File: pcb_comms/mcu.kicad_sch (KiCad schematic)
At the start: 28 parts, among them U2 STM32WLE5CCU6, Y3 32MHz

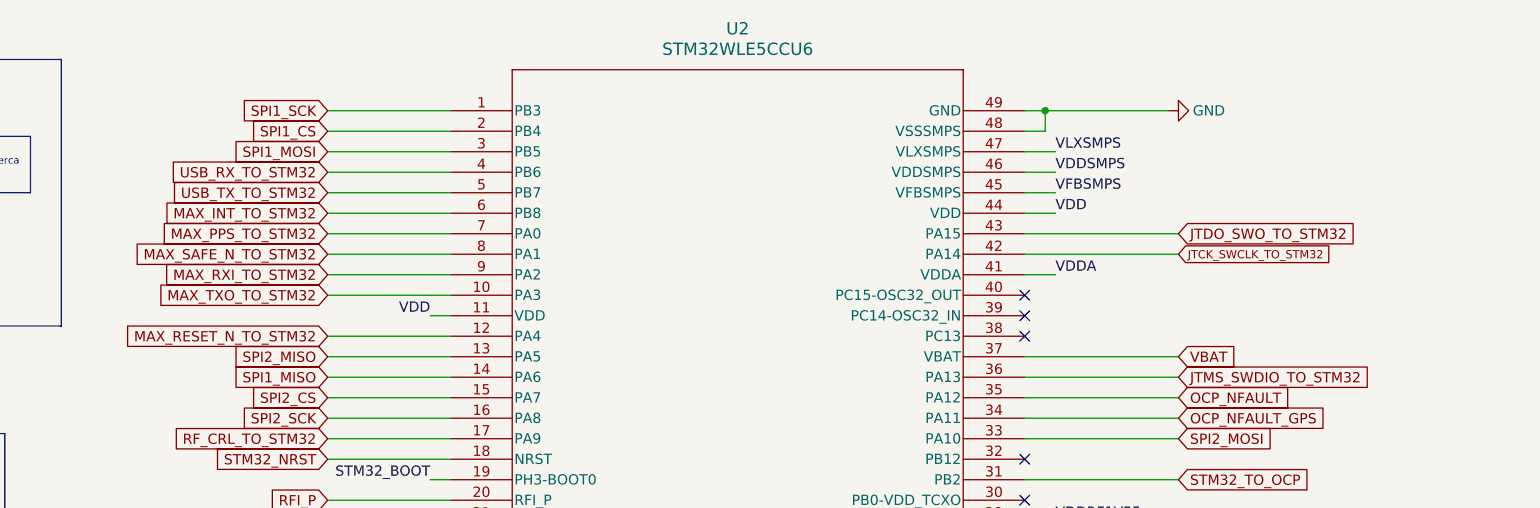
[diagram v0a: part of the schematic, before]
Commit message: Add DRA818
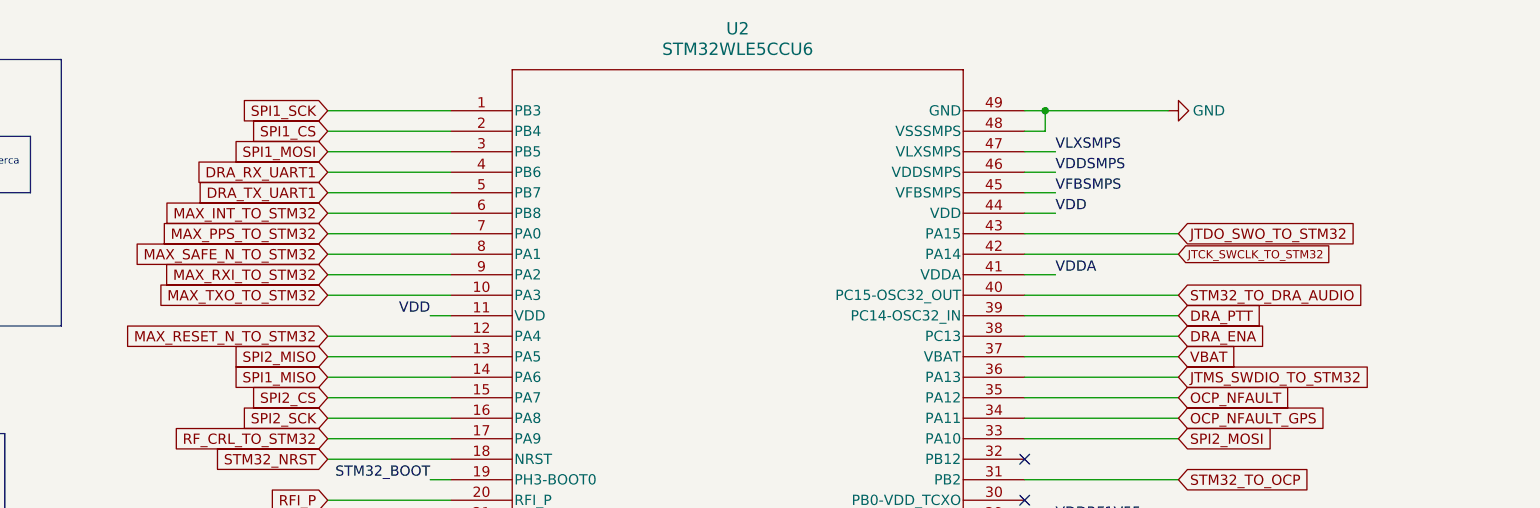
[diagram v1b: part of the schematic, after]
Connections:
- net DRA_ENA: now reaches U2.38 (PC13)
- net DRA_PTT: now reaches U2.39 (PC14-OSC32_IN)
- net STM32_TO_DRA_AUDIO: now reaches U2.40 (PC15-OSC32_OUT)
- net USB_RX_TO_STM32 renamed DRA_RX_UART1
- net USB_TX_TO_STM32 renamed DRA_TX_UART1
- no-connect marks 6 -> 3

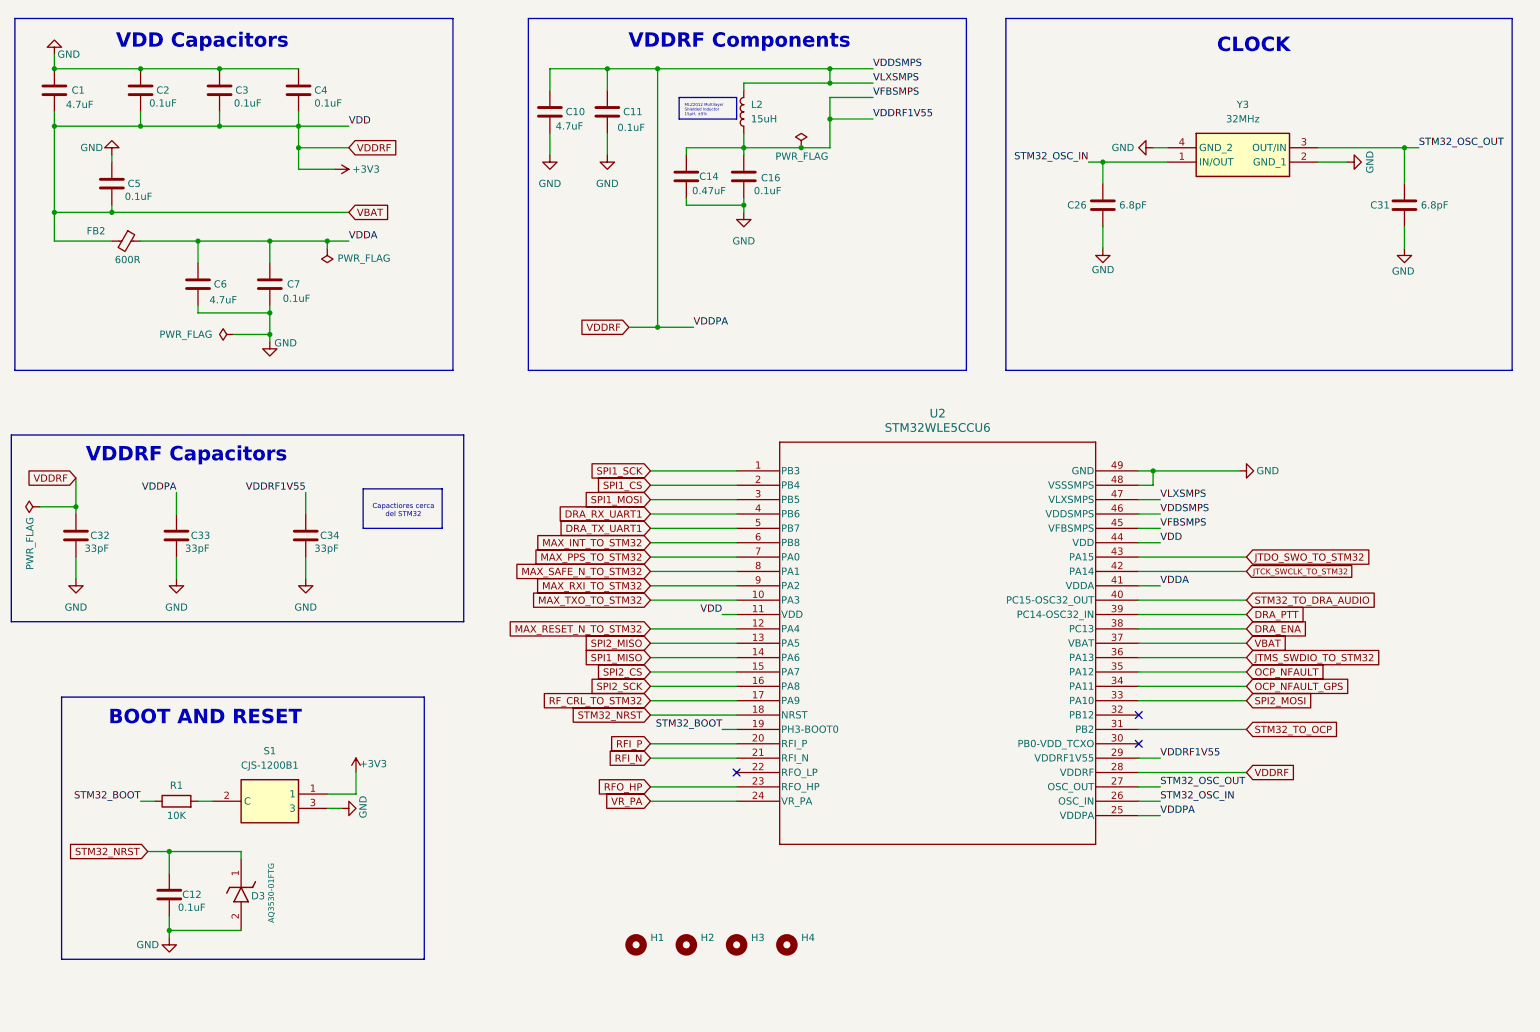
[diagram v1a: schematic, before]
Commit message: remove gps
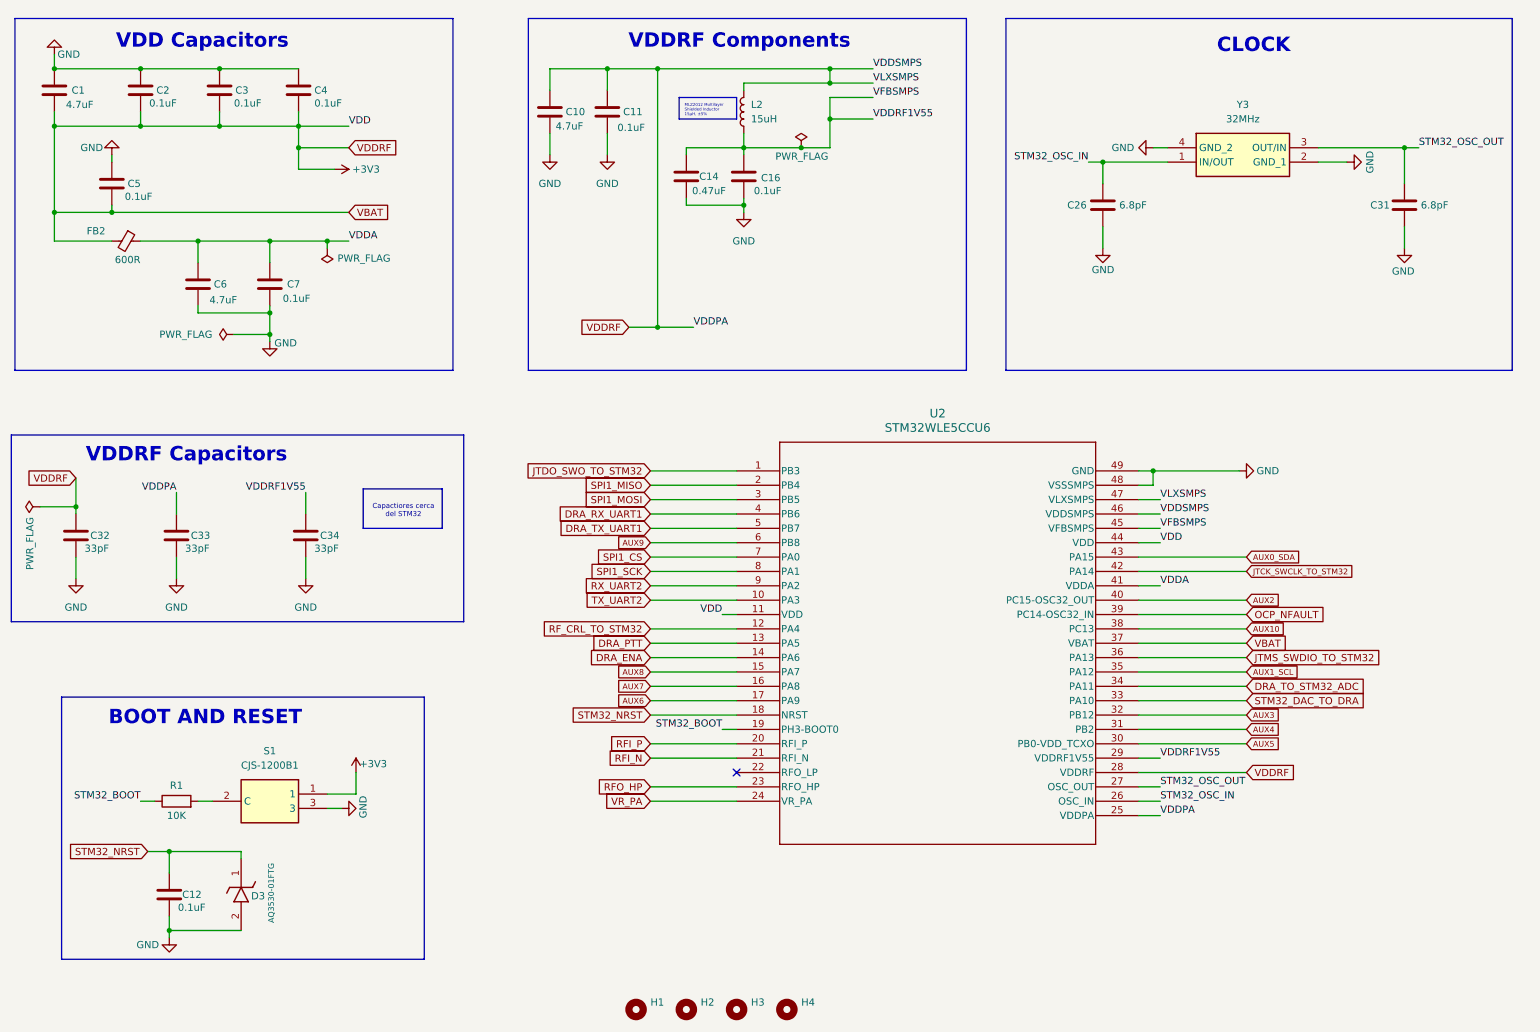
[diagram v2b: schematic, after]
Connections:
- net MAX_PPS_TO_STM32 is gone; now on net SPI1_CS: U2.7 (PA0)
- net MAX_RESET_N_TO_STM32 is gone; now on net RF_CRL_TO_STM32: U2.12 (PA4)
- net MAX_SAFE_N_TO_STM32 is gone; now on net SPI1_SCK: U2.8 (PA1)
- net SPI2_MISO is gone; now on net DRA_PTT: U2.13 (PA5)
- net DRA_ENA: now also U2.14 (PA6); no longer U2.38 (PC13)
- net DRA_PTT: no longer U2.39 (PC14-OSC32_IN)
- net JTDO_SWO_TO_STM32: now also U2.1 (PB3); no longer U2.43 (PA15)
- net OCP_NFAULT: now also U2.39 (PC14-OSC32_IN); no longer U2.35 (PA12)
- net RF_CRL_TO_STM32: no longer U2.17 (PA9)
- net SPI1_CS: no longer U2.2 (PB4)
- net SPI1_MISO: now also U2.2 (PB4); no longer U2.14 (PA6)
- net SPI1_SCK: no longer U2.1 (PB3)
- net AUX5: now reaches U2.30 (PB0-VDD_TCXO)
- net AUX3: now reaches U2.32 (PB12)
- net MAX_INT_TO_STM32 renamed AUX9
- net MAX_RXI_TO_STM32 renamed RX_UART2
- net MAX_TXO_TO_STM32 renamed TX_UART2
- net OCP_NFAULT_GPS renamed DRA_TO_STM32_ADC
- net SPI2_CS renamed AUX8
- net SPI2_MOSI renamed STM32_DAC_TO_DRA
- net SPI2_SCK renamed AUX7
- net STM32_TO_DRA_AUDIO renamed AUX2
- net STM32_TO_OCP renamed AUX4
- new net AUX0_SDA: U2.43 (PA15)
- new net AUX10: U2.38 (PC13)
- new net AUX1_SCL: U2.35 (PA12)
- new net AUX6: U2.17 (PA9)
- no-connect marks 3 -> 1
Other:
- moved on the sheet: H1, H2, H3, H4

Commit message: Update pinout
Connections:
- net RX_UART2 is gone; now on net DRA_RX_UART1: U2.9 (PA2)
- net TX_UART2 is gone; now on net DRA_TX_UART1: U2.10 (PA3)
- net DRA_ENA renamed STM32_TO_DRA_PTT
- net DRA_PTT renamed DRA_SQ_TO_STM32

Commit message: Update pinout 2
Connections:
- net DRA_RX_UART1: no longer U2.9 (PA2)
- net DRA_TX_UART1: no longer U2.10 (PA3)
- new net USB_RX_UART2: U2.9 (PA2)
- new net USB_TX_UART2: U2.10 (PA3)

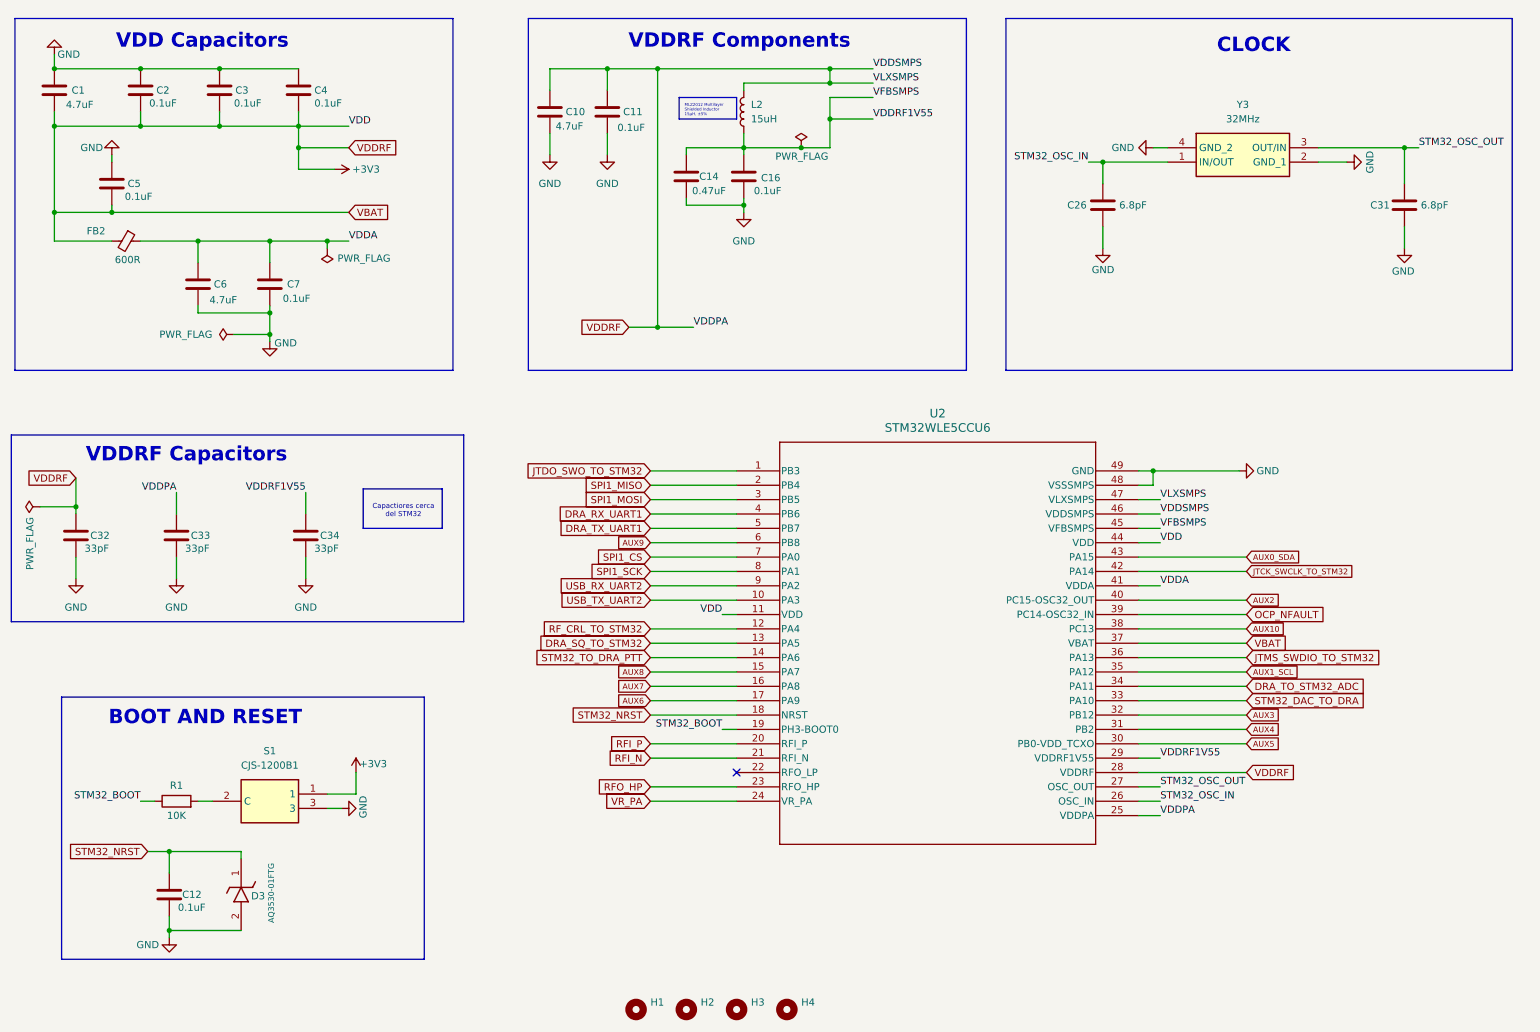
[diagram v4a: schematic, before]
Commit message: Update schematic. Add net classes and JST footprints for aux
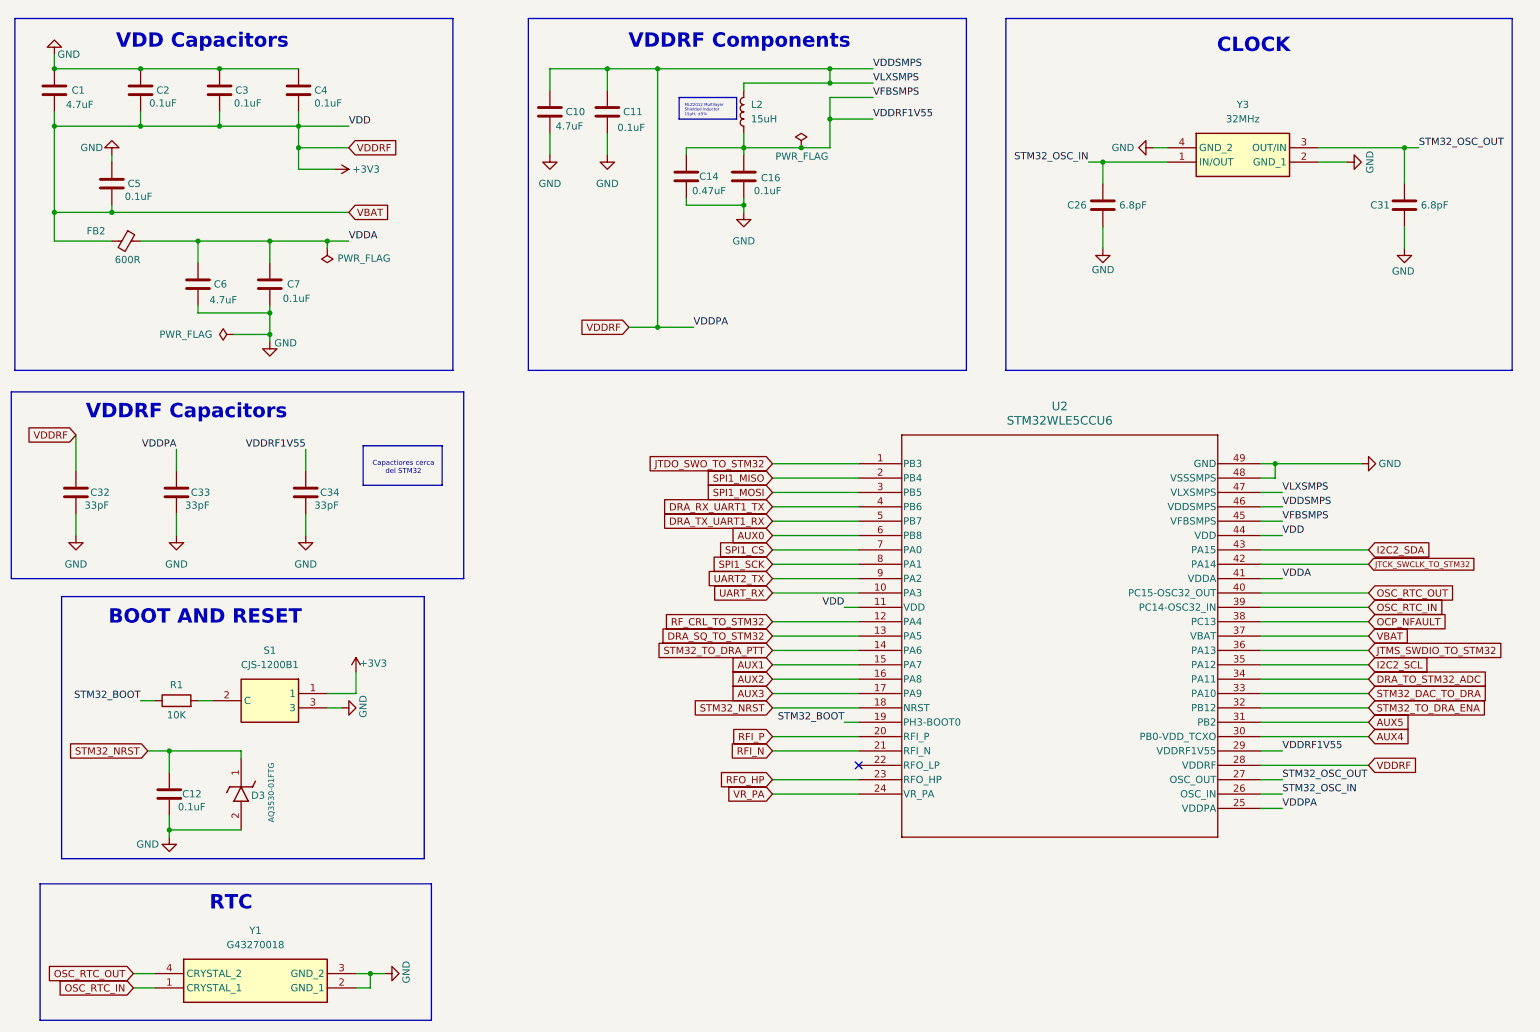
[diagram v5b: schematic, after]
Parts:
- removed H1, H2, H3, H4: MountingHole, MountingHole:MountingHole_3.2mm_M3_Pad_Via, symbol Mechanical:MountingHole
- added Y1: G43270018, CRYSTAL_32.687KHz_G43270018:CRYSTAL_32.687KHz_G43270018, symbol CRYSTAL_32.687KHz_G43270018:G43270018
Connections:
- net AUX10 is gone; now on net OCP_NFAULT: U2.38 (PC13)
- net AUX6 is gone; now on net AUX3: U2.17 (PA9)
- net AUX7 is gone; now on net AUX2: U2.16 (PA8)
- net AUX2: no longer U2.40 (PC15-OSC32_OUT)
- net AUX3: no longer U2.32 (PB12)
- net AUX4: now also U2.30 (PB0-VDD_TCXO); no longer U2.31 (PB2)
- net AUX5: now also U2.31 (PB2); no longer U2.30 (PB0-VDD_TCXO)
- net GND: now also Y1.2 (GND_1), Y1.3 (GND_2)
- net OCP_NFAULT: no longer U2.39 (PC14-OSC32_IN)
- net AUX0_SDA renamed I2C2_SDA
- net AUX1_SCL renamed I2C2_SCL
- net AUX8 renamed AUX1
- net AUX9 renamed AUX0
- net DRA_RX_UART1 renamed DRA_RX_UART1_TX
- net DRA_TX_UART1 renamed DRA_TX_UART1_RX
- net USB_RX_UART2 renamed UART2_TX
- net USB_TX_UART2 renamed UART_RX
- new net OSC_RTC_IN: U2.39 (PC14-OSC32_IN), Y1.1 (CRYSTAL_1)
- new net OSC_RTC_OUT: U2.40 (PC15-OSC32_OUT), Y1.4 (CRYSTAL_2)
- new net STM32_TO_DRA_ENA: U2.32 (PB12)
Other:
- note added: "RTC"
- moved on the sheet: C12, C32, C33, C34, D3, R1, S1, U2
